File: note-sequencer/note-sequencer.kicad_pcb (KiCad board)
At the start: 2 copper layers, 160.9 x 383.9 mm, 133 parts, among them J1 Pitch, J10 Velocity, J11 Pitch, J12 Clock, J13 Gate, J14 LED Socket, J2 Gate, J3 Velocity, J4 Clock, J5 Power, J6 Power, J7 Power, J8 Conn_01x06_Socket, J9 Conn_01x06_Pin, SW1 C1, SW10 A1, SW11 A#1, SW12 B1, SW13 C2, SW14 C#2, SW15 D2, SW16 D#2, SW17 E2, SW18 F2, SW19 F#2, SW2 C#1, SW20 G2, SW21 G#2, SW22 A2, SW23 A#2, SW24 B2, SW25 C3, SW26 X1, SW27 X2, SW28 X3, SW29 X4, SW3 D1, SW30 SW_DIP_x01, SW31 RotaryEncoder_Switch, SW32 C2, SW33 Clock Source, SW34 SW_DIP_x01, SW35 Mode, SW4 D#1, SW5 E1, SW6 F1, SW6 X5, SW7 F#1, SW8 G1, SW9 G#1, U4 TL072

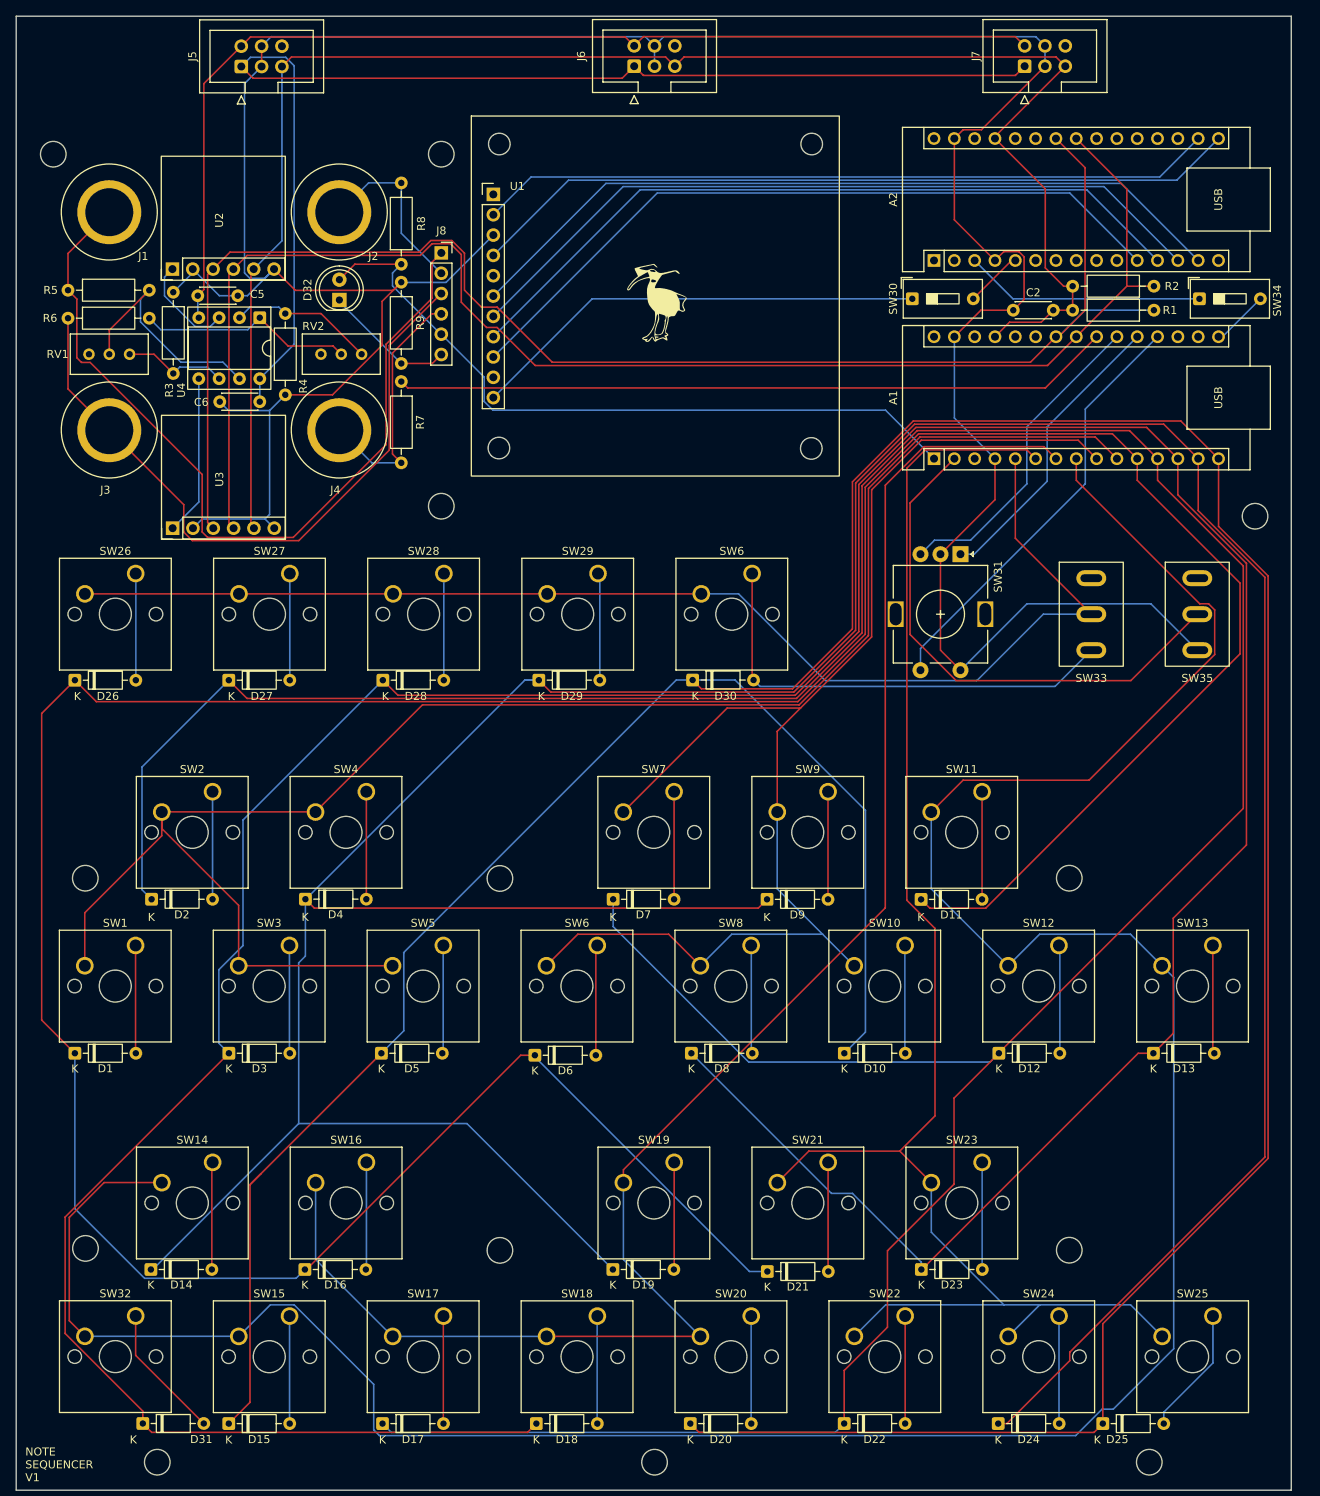
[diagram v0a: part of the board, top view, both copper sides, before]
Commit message: Renumber some components
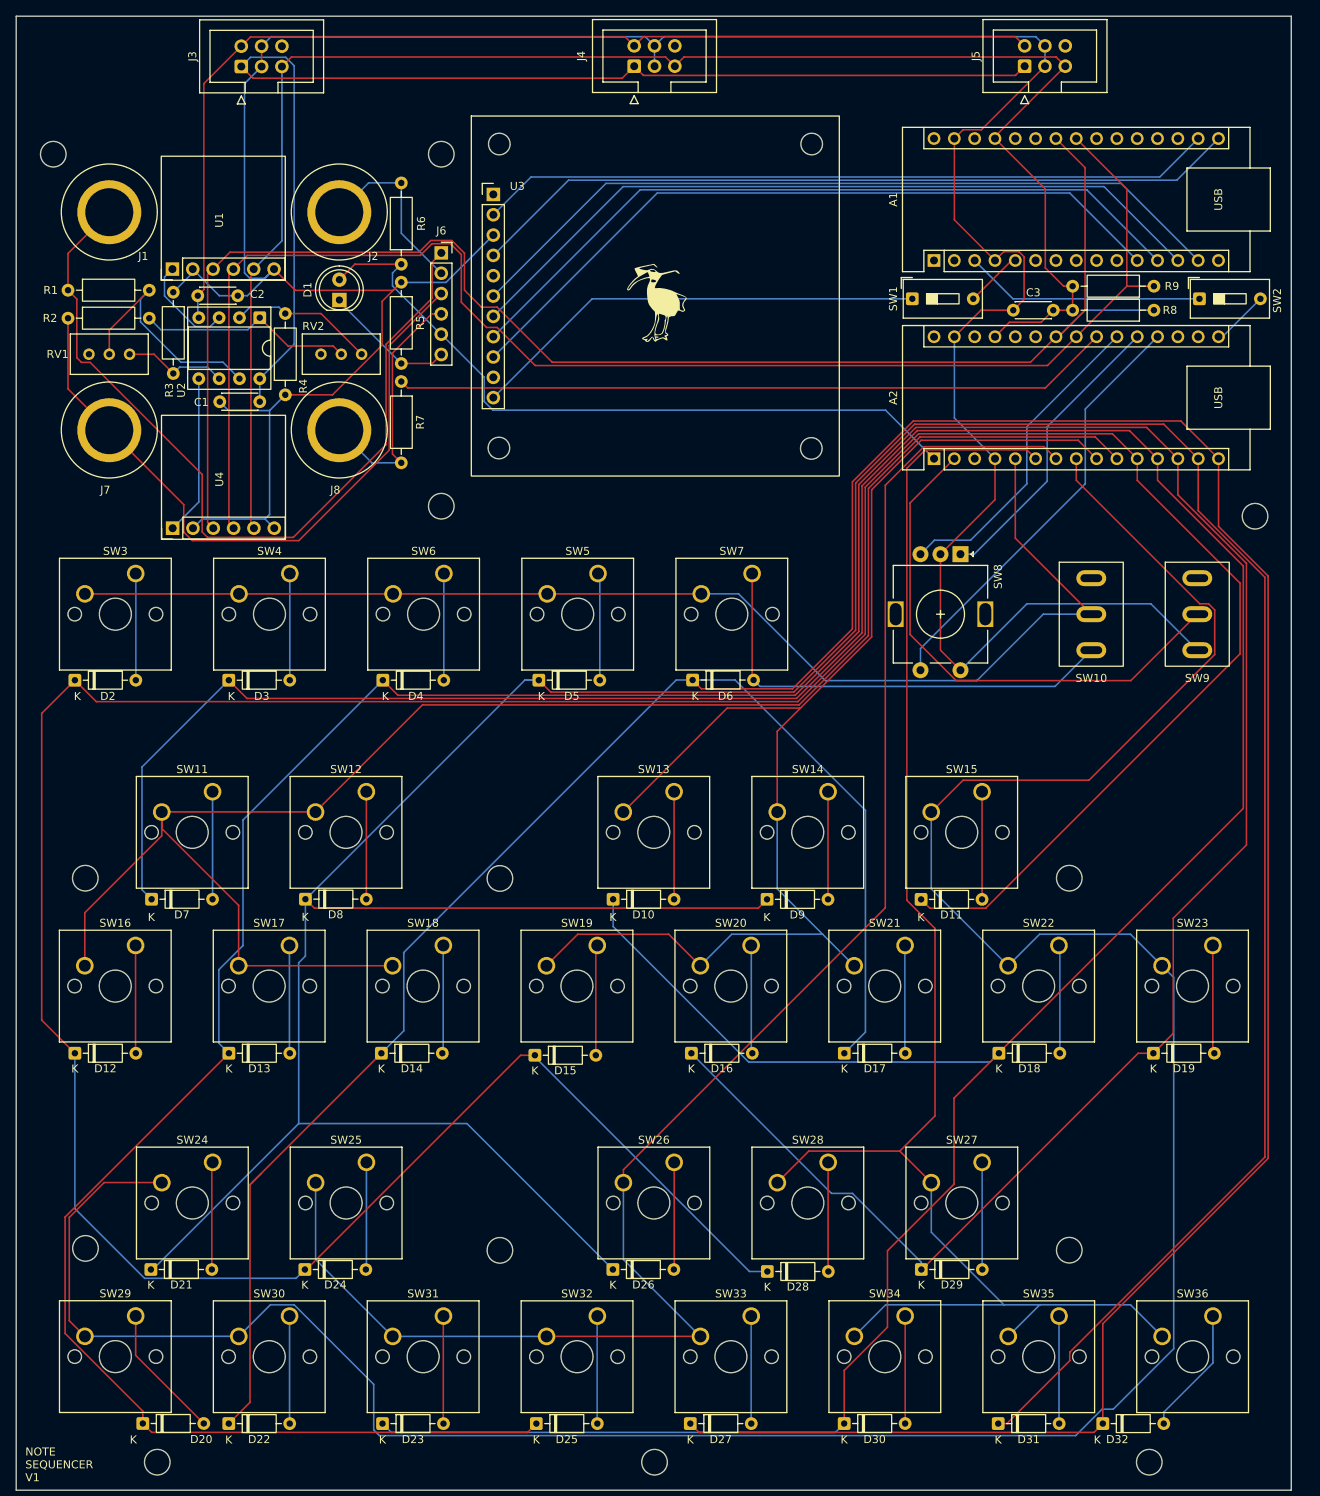
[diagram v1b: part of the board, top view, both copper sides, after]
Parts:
- renumbered A2 to A1, A1 to A2, C6 to C1, C5 to C2, C2 to C3, D32 to D1, D7 to D10, D1 to D12, D3 to D13, D5 to D14, D6 to D15, D8 to D16, D10 to D17, D12 to D18, D13 to D19, D26 to D2, D31 to D20, D14 to D21, D15 to D22, D17 to D23, D16 to D24, D18 to D25, D19 to D26, D20 to D27, D21 to D28, D23 to D29, D27 to D3, D22 to D30, D24 to D31, D25 to D32, D28 to D4, D29 to D5, D30 to D6, D2 to D7, D4 to D8, J13 to J10, J10 to J11, J14 to J13, J9 to J14, J5 to J3, J6 to J4, J7 to J5, J8 to J6, J3 to J7, J4 to J8, J11 to J9, R5 to R1, R6 to R2, R9 to R5, R8 to R6, R1 to R8, R2 to R9, SW30 to SW1, SW33 to SW10, SW2 to SW11, SW4 to SW12, SW7 to SW13, SW9 to SW14, SW11 to SW15, SW1 to SW16, SW3 to SW17, SW5 to SW18, SW6 to SW19, SW34 to SW2, SW8 to SW20, SW10 to SW21, SW12 to SW22, SW13 to SW23, SW14 to SW24, SW16 to SW25, SW19 to SW26, SW23 to SW27, SW21 to SW28, SW32 to SW29, SW26 to SW3, SW15 to SW30, SW17 to SW31, SW18 to SW32, SW20 to SW33, SW22 to SW34, SW24 to SW35, SW25 to SW36, SW27 to SW4, SW29 to SW5, SW28 to SW6, SW6 to SW7, SW31 to SW8, SW35 to SW9, U2 to U1, U4 to U2, U1 to U3, U3 to U4

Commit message: Revert "Renumber some components"
This reverts commit 4c9a93e4336de2276d9b49e02718b6a92f997a6a.
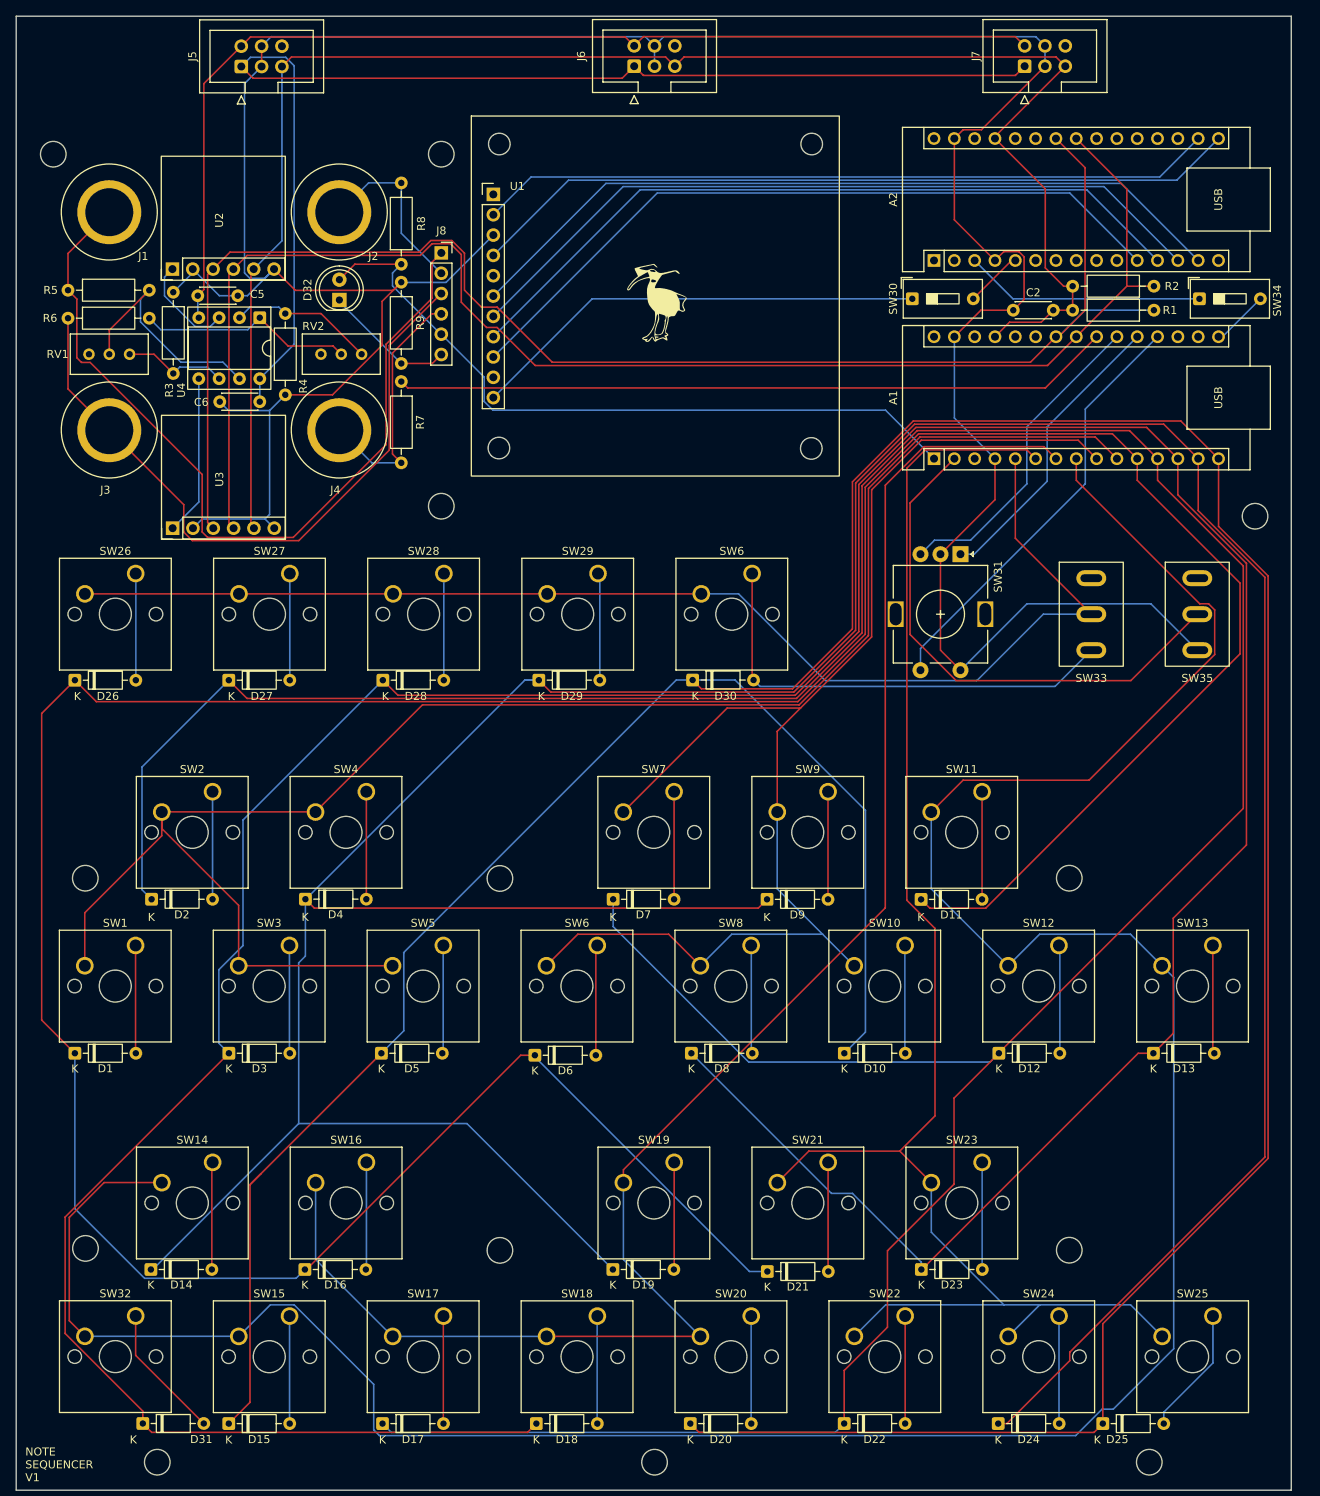
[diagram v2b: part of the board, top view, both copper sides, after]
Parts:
- renumbered A2 to A1, A1 to A2, C3 to C2, C2 to C5, C1 to C6, D12 to D1, D17 to D10, D18 to D12, D19 to D13, D21 to D14, D22 to D15, D24 to D16, D23 to D17, D25 to D18, D26 to D19, D7 to D2, D27 to D20, D28 to D21, D30 to D22, D29 to D23, D31 to D24, D32 to D25, D2 to D26, D3 to D27, D4 to D28, D5 to D29, D13 to D3, D6 to D30, D20 to D31, D1 to D32, D8 to D4, D14 to D5, D15 to D6, D10 to D7, D16 to D8, J11 to J10, J9 to J11, J10 to J13, J13 to J14, J7 to J3, J8 to J4, J3 to J5, J4 to J6, J5 to J7, J6 to J8, J14 to J9, R8 to R1, R9 to R2, R1 to R5, R2 to R6, R6 to R8, R5 to R9, SW16 to SW1, SW21 to SW10, SW15 to SW11, SW22 to SW12, SW23 to SW13, SW24 to SW14, SW30 to SW15, SW25 to SW16, SW31 to SW17, SW32 to SW18, SW26 to SW19, SW11 to SW2, SW33 to SW20, SW28 to SW21, SW34 to SW22, SW27 to SW23, SW35 to SW24, SW36 to SW25, SW3 to SW26, SW4 to SW27, SW6 to SW28, SW5 to SW29, SW17 to SW3, SW1 to SW30, SW8 to SW31, SW29 to SW32, SW10 to SW33, SW2 to SW34, SW9 to SW35, SW12 to SW4, SW18 to SW5, SW7 to SW6, SW19 to SW6, SW13 to SW7, SW20 to SW8, SW14 to SW9, U3 to U1, U1 to U2, U4 to U3, U2 to U4
